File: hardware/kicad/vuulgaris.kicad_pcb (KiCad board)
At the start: 4 copper layers, 284.3 x 116.8 mm, 291 parts, among them J1 TFPUSH, J10 PJ-603_C41409498, J11 TYPE-C-31-M-12, J12 FACEPLATE 2x5 IDC, J2 PJ-376, J3 PJ-376, J4 PJ-376, J5 PJ-376, J6 PJ-376, J7 PJ-603_C41409498, J8 PJ-603_C41409498, J9 PJ-603_C41409498, Q1 J113 / MMBFJ113, Q2 J113 / MMBFJ113, SW1 SW_DPDT_FLAT, SW2 SW_DPDT_FLAT, SW4 12x12 tactile, SW5 12x12 tactile, SW6 12x12 tactile, SW7 12x12 tactile, SW8 12x12 tactile, SW9 12x12 tactile, U1 ES_DAISY_PATCH_SM_REV1, U101 V3205SD, U102 TL072_FLAT, U103 TL072_FLAT, U104 CD4046B, U106 TL072_FLAT, U201 V3205SD, U202 TL072_FLAT, U203 TL072_FLAT, U204 CD4046B, U206 TL072_FLAT, U3 MCP23017-E_SO, U301 TL084, U302 TL074, U4 MCP23017-E_SO, U401 TL084, U402 TL074, U5 AMS1117-3.3, U6 AMS1117-3.3, U7 DKM10E-12, U8 78L05, U9 OPA1688_FLAT

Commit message: hardware: 13 back-side parts had the FRONT land pattern -- fixed
Placing the preamp turned up a disagreement between my slot finder and
place.py, and chasing it found a board-killing bug that predates both.

KiCad applies no implicit mirror. Proven with kicad-cli pcb export svg: a pad
at footprint-local (0,+3) plots to the same absolute position whether its
footprint is on F.Cu or B.Cu. Front and back render identically, so the flip
has to be baked into the stored coordinates.

Thirteen parts on B.Cu still matched the library exactly, meaning they were
never mirrored -- only their layer names were rewritten. Q1, Q2, U101-U106 and
U201-U206: both V3205SD bucket brigades, both CD4046 clocks, five of six
TL072s, both transistors. The whole analogue block, every one of them soldered
mirror-image with pin 1 in the wrong corner.

Nothing caught it because place.py was applying an extra mirror of its own in
the position maths, so a half-flipped part measured correct -- two errors
cancelling inside the checks. The old comment claimed Gerber verification
against J7 and J11, but J7 is correctly mirrored and J11 is on the front, so
that check compared a double mirror against a single one. Meanwhile the pad
ANGLE check in the same file already assumed baked-in mirroring; the two halves
of place.py had contradicted each other for months.

Fixed: mir removed from place.py's position maths, the flip completed on all
106 half-flipped B.Cu footprints, and a new check that names any B.Cu footprint
whose asymmetric pads still match the library. Verified by half-flipping U102
on purpose and confirming the guard fires.

C507/C508 and RT502 re-placed against the corrected geometry. All 28 bypass
caps now within 5.0mm, pad overlaps none, body overlaps back to the
pre-existing four, 939/939 connections verified.
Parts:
- added C509: 100nF, vuulgaris:C0603, B.Cu at (280.6, 92.9)
- added C510: 100nF, vuulgaris:C0603, B.Cu at (272.3, 86.5)
- added C511: 1uF film, vuulgaris:C0603, B.Cu at (272.3, 89.9)
- added C512: 1uF film, vuulgaris:C0603, B.Cu at (280.7, 84.1)
- added R513: 1k3, vuulgaris:R0603, B.Cu at (310.5, 76.0)
- added R514: 1k, vuulgaris:R0603, B.Cu at (307.0, 76.0)
- added R515: 1k3, vuulgaris:R0603, B.Cu at (325.5, 76.0)
- added R516: 1k, vuulgaris:R0603, B.Cu at (322.0, 76.0)
- added R517: 1k, vuulgaris:R0603, B.Cu at (267.7, 78.5)
- added R518: 1k, vuulgaris:R0603, B.Cu at (286.7, 78.5)
- added R519: 100k, vuulgaris:R0603, B.Cu at (273.8, 83.4)
- added R520: 100k, vuulgaris:R0603, B.Cu at (283.7, 86.6)
- added R521: 2k2, vuulgaris:R0603, B.Cu at (275.3, 93.1)
- added R522: 2k2, vuulgaris:R0603, B.Cu at (283.7, 90.4)
- added RT503: 20k trim, vuulgaris:RES-ADJ-SMD_3224W, B.Cu at (268.8, 89.1)
- added RT504: 20k trim, vuulgaris:RES-ADJ-SMD_3224W, B.Cu at (287.2, 87.9)
- added U10: OPA1688_FLAT, vuulgaris:SOP-8_L4.9-W3.9-P1.27-LS6.0-BL, B.Cu at (278.0, 88.5)
- R511, R512: value 22R -> 4R7
- moved RT502 17.4 mm to (337.6, 73.7)
- moved C507 8.03 mm to (339.2, 69.5), turned to 0 degrees
- moved C508 5.46 mm to (348.2, 62.2)
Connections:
- C501 pad 1: /EXT_IN_L -> /EXT_AMP_OUT_L
- C502 pad 1: /EXT_IN_R -> /EXT_AMP_OUT_R
- J10 pad 4: /BBD_OUT_R -> /LINE_OUT_R
- J9 pad 4: /BBD_OUT_L -> /LINE_OUT_L
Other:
- board size 284.3 x 116.8 mm -> 284.3 x 326.3 mm

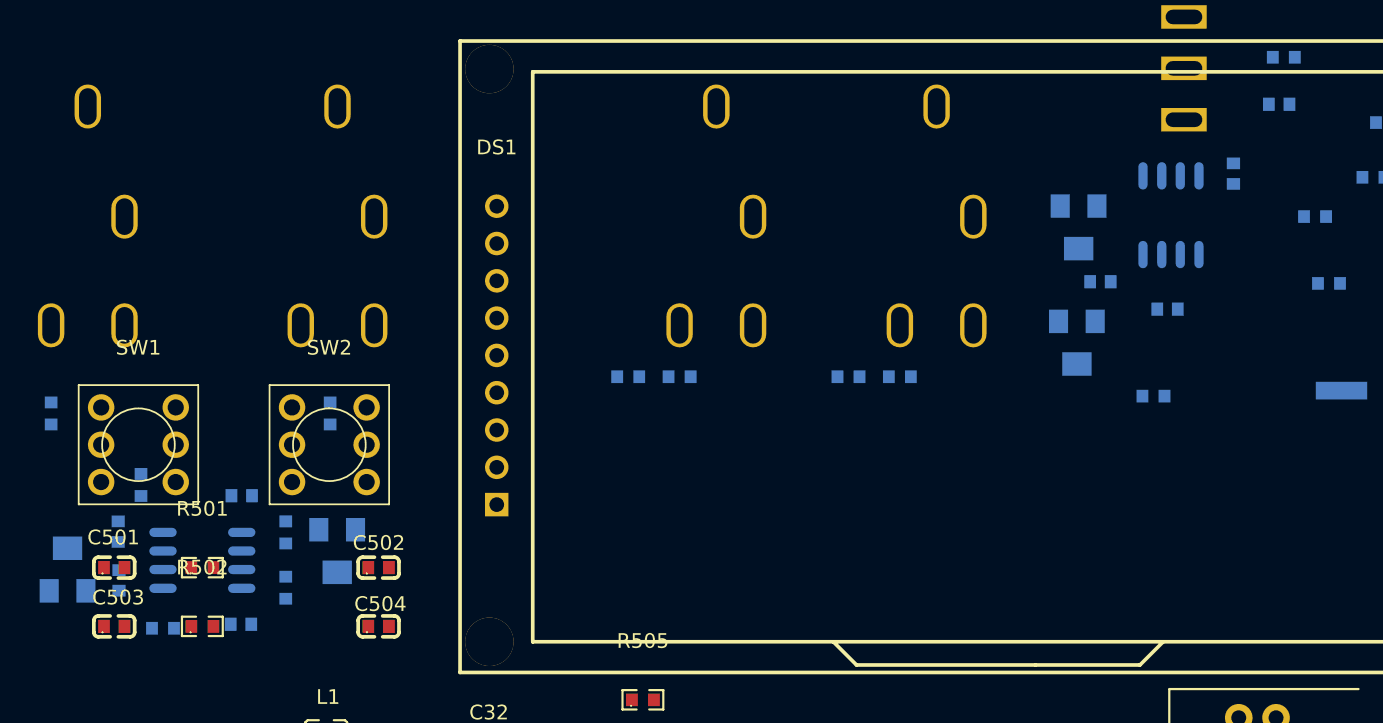
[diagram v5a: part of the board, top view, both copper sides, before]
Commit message: hardware: the 1uF "film" caps are 0805 X7R, because film was never possible
Fourteen caps carried the value "1uF film" in an 0603 footprint, which is not a
shippable part. SMD film tops out near 0.1uF in 1210; 1uF film is a leaded box
cap about 7x7mm on a 5mm pitch, hand-soldered, on a board whose hand-solder list
was cut to four genuinely unsourceable parts. What would actually have been
assembled is a Class II MLCC, so the value string was describing a wish.

They are now 1uF X7R 50V in C0805. Renaming alone would have been honest but
would have left the distortion: Class II voltage-coefficient nonlinearity scales
with the field across the dielectric, and a 1uF 50V part in 0805 has more and
thicker layers than a 1uF 16V part in 0603 being asked to swing a third of its
rating on a +/-4.75V Eurorack signal. 1uF C0G is the linear answer and is not an
option -- nothing below 2220, a few dollars each, fourteen of them would swallow
the board.

Eleven took the bigger footprint where they stood, checked against the corrected
back-side geometry. C505 turns 90 degrees to clear J6's body, C511 moves 3.4mm,
C512 0.25mm.

939/939 connections verified, all 28 bypass caps inside 5.0mm, no pad overlaps,
same-face body overlaps back to the pre-existing four.
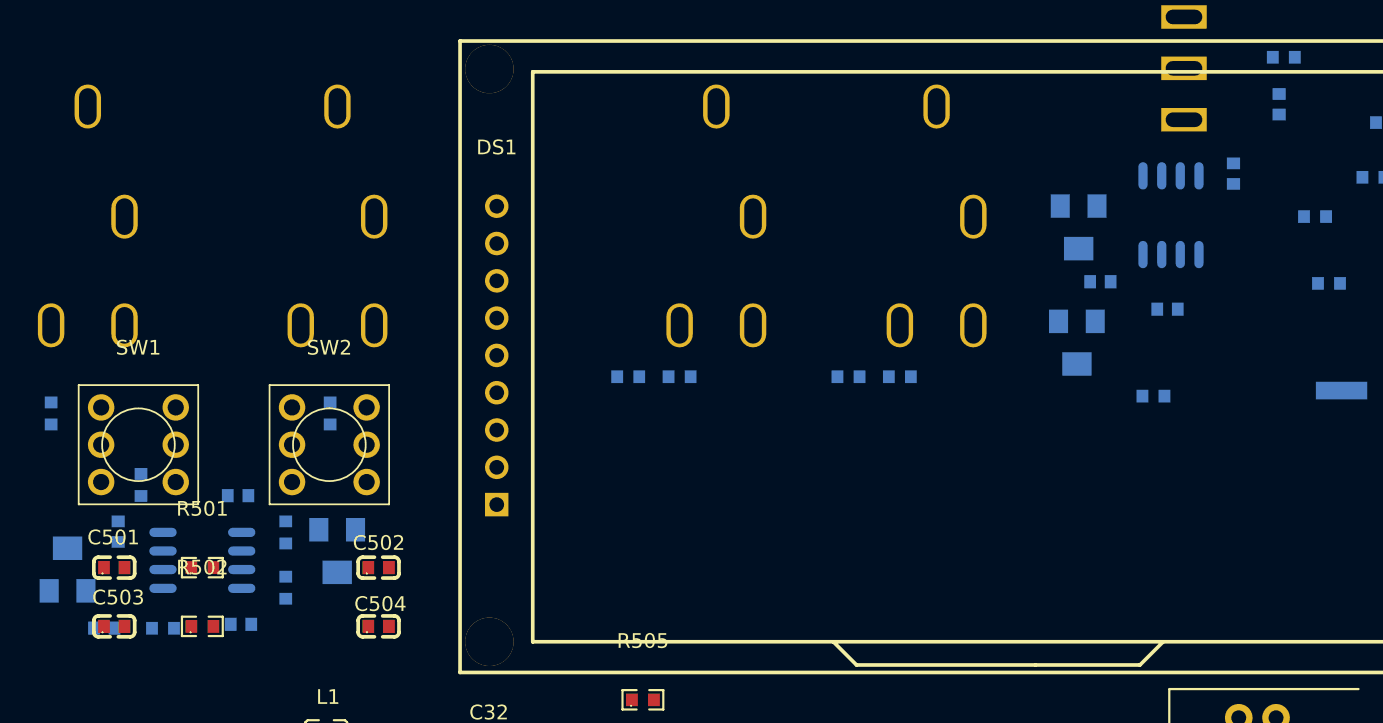
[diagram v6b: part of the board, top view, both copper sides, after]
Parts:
- moved C511 3.40 mm to (271.3, 93.1), turned to 0 degrees
- moved C512 0.25 mm to (280.4, 84.1)
- turned C505 to 90 degrees
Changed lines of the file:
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@@
   )
   (footprint "vuulgaris:C0603" (layer "B.Cu")
-    (at 280.68 84.1)
+    (at 280.43 84.1)
     (property "Sheetfile" "vuulgaris.kicad_sch")
     (property "Sheetname" "")
@@
   )
   (footprint "vuulgaris:C0603" (layer "B.Cu")
-    (at 272.32 89.87 90)
+    (at 271.32 93.12)
     (property "Sheetfile" "vuulgaris.kicad_sch")
     (property "Sheetname" "")
@@
     (fp_line (start 0.8 -0.4) (end -0.8 -0.4)
       (stroke (width 0.05) (type solid)) (layer "B.CrtYd"))
-    (pad "1" smd rect (at -0.7 0 90) (size 0.8 0.9) (layers "B.Cu" "B.Paste" "B.Mask")
+    (pad "1" smd rect (at -0.7 0) (size 0.8 0.9) (layers "B.Cu" "B.Paste" "B.Mask")
       (net 265 "/EXT_PROT_L") (pintype "passive"))
-    (pad "2" smd rect (at 0.7 0 90) (size 0.8 0.9) (layers "B.Cu" "B.Paste" "B.Mask")
+    (pad "2" smd rect (at 0.7 0) (size 0.8 0.9) (layers "B.Cu" "B.Paste" "B.Mask")
       (net 264 "/EXT_AMP_IN_L") (pintype "passive"))
     (model "lib/vuulgaris.3dshapes/C0603_L1.6-W0.8-H0.8.wrl"
@@
   )
   (footprint "vuulgaris:C0603" (layer "B.Cu")
-    (at 351.326 57.446)
+    (at 351.326 57.446 90)
     (property "Sheetfile" "vuulgaris.kicad_sch")
     (property "Sheetname" "")
@@
     (fp_line (start 0.8 0.4) (end 0.8 -0.4)
       (stroke (width 0.05) (type solid)) (layer "B.CrtYd"))
-    (pad "1" smd rect (at -0.7 0) (size 0.8 0.9) (layers "B.Cu" "B.Paste" "B.Mask")
+    (pad "1" smd rect (at -0.7 0 90) (size 0.8 0.9) (layers "B.Cu" "B.Paste" "B.Mask")
       (net 183 "/BBD_OUT_L") (pintype "passive"))
-    (pad "2" smd rect (at 0.7 0) (size 0.8 0.9) (layers "B.Cu" "B.Paste" "B.Mask")
+    (pad "2" smd rect (at 0.7 0 90) (size 0.8 0.9) (layers "B.Cu" "B.Paste" "B.Mask")
       (net 252 "/HP_IN_L") (pintype "passive"))
     (model "lib/vuulgaris.3dshapes/C0603_L1.6-W0.8-H0.8.wrl"

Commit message: hardware: restore the board outline -- pose.py had negated Edge.Cuts
The faceplate connector cutout lost its four straight edges. My unmirror pass
and pose.py split the board file into footprints by "start of one to start of
the next, with end-of-file as the last boundary", so the LAST footprint's block
ran to EOF and swallowed everything after it: Edge.Cuts, the zone, all of it.
The mirror transform then negated Y on all eight gr_line segments -- the outer
rectangle and the cutout both.

The four gr_arc corners survived because the negation regex wanted
(start ...) (end ...) adjacent and an arc carries a (mid ...) between them. So
the cutout kept its rounded corners and lost its edges, which is why nothing
automated caught it. Dylan spotted it by looking at the board.

place.py's fp_blocks walks to the balanced closing paren and always had this
right; pose.py rolled its own. pose.py now uses the balanced walk.

The same bug was also silently dropping pose.py's writes: it reported restoring
C505:rot90 and C511:rot0 and the board did not change. With the splitter fixed
those apply, and J1 -- which had been knocked to -90 in the working tree and is
rot 90 in every commit back to bda23e2 -- is back where it belongs.

Edge.Cuts restored from 7568060, the commit before the unmirror pass. Verified
surgical: only those 8 lines differ, 308 footprints on both sides.

outer rectangle x100-384.3 y50-166.81, cutout x310-334 y147.5-159.5, no
negative Y anywhere. place.py: clear of the cutout, pads inside the outline,
every B.Cu footprint mirrored, all 28 bypass caps inside 5.0mm, no pad
overlaps. pose.py --check: 0 drifted. 939/939 connections verified.
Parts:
- moved R519 7.55 mm to (266.3, 83.5)
- moved RT503 3.27 mm to (265.9, 90.6)
- moved C510 2.60 mm to (272.5, 89.1)
- moved R521 2.60 mm to (275.6, 95.7)
- moved C501 2.60 mm to (272.2, 91.6)
- moved C502 2.60 mm to (290.2, 91.6)
- moved C503 2.60 mm to (272.2, 95.6)
- moved C504 2.60 mm to (290.2, 95.6)
- moved C509 2.60 mm to (280.9, 95.4)
- moved R501 2.60 mm to (278.2, 91.6)
- moved R502 2.60 mm to (278.2, 95.6)
- moved R520 2.60 mm to (283.9, 89.2)
- moved U10 2.60 mm to (278.2, 91.1)
- moved R522 2.60 mm to (283.9, 93.0)
- moved RT504 2.60 mm to (287.4, 90.5)
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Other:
- board size 284.3 x 326.3 mm -> 284.3 x 116.8 mm

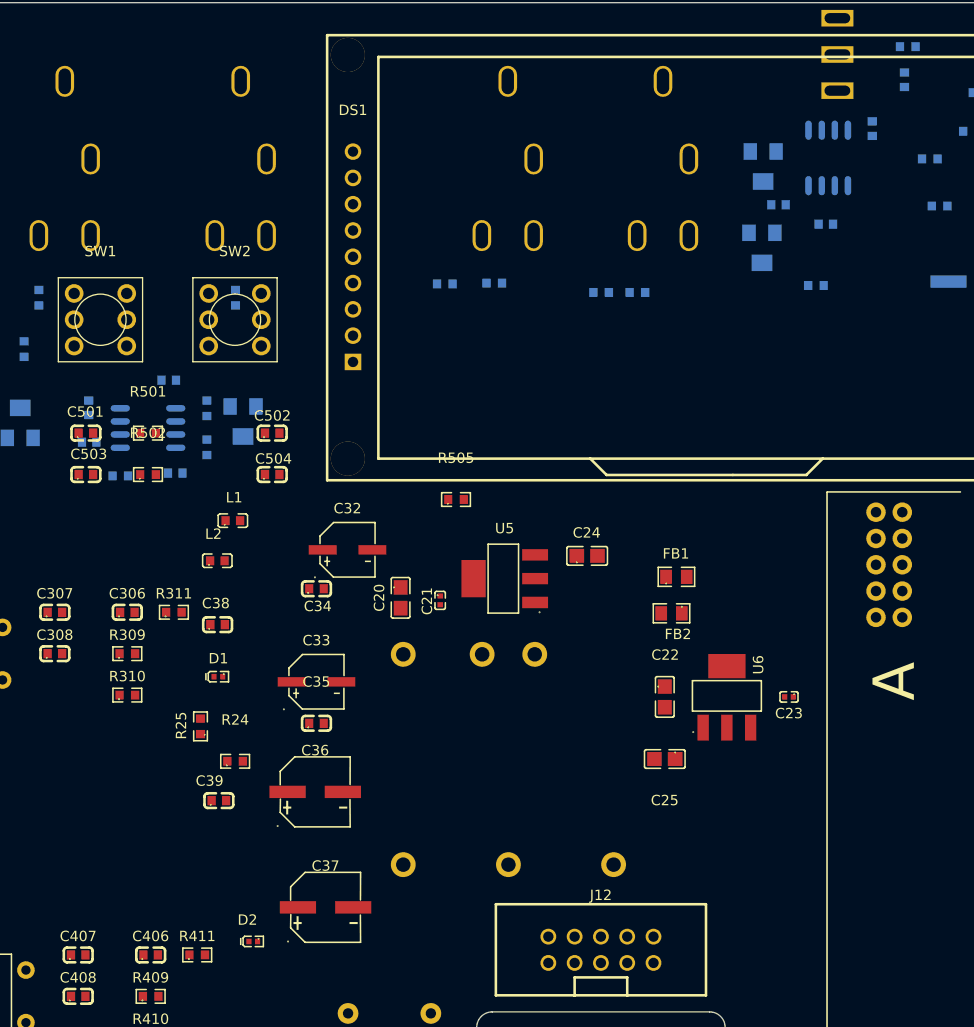
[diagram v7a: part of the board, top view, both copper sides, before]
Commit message: hardware: repair the board outline again, and guard it this time
The F8 wrote the damaged Edge.Cuts back. Commit f5b0823 had it correct on disk,
but Pcbnew was still holding the board it loaded before that fix, and saving
wrote its snapshot over the repair -- the snapshot I took immediately after the
F8, before running any tool, already has the negative Y. Fourth time the stale
in-memory board has cost work, and the first time it silently undid a fix.

What that looks like from the outside is an outline that needs moving: parts at
y 50-167, outline at y -50 to -167, drawn nowhere near the board.

Edge.Cuts sign-flipped back. place.py now validates the outline BEFORE measuring
anything against it -- negative coordinates, or most footprints falling outside
it, and it says so and says why it matters. "pads inside the outline" passes
trivially when the outline is somewhere else entirely, which is exactly how this
went unnoticed. Verified by re-breaking Edge.Cuts on purpose and confirming it
fires, then restoring.

Also C511 came out of the F8 0.36mm from U10 -- it was in free-placement.json,
so "board wins" kept the F8's position rather than the seed. Dropped and
re-seeded at 2.06mm.

board outline x 100..384.3 y 50..166.81, 1 interior cutout. All 14 coupling caps
swapped to C0805. 939/939 connections verified, all 28 bypass caps within 5.0mm,
no pad overlaps, back to the 11 pre-existing sub-1mm pairs.
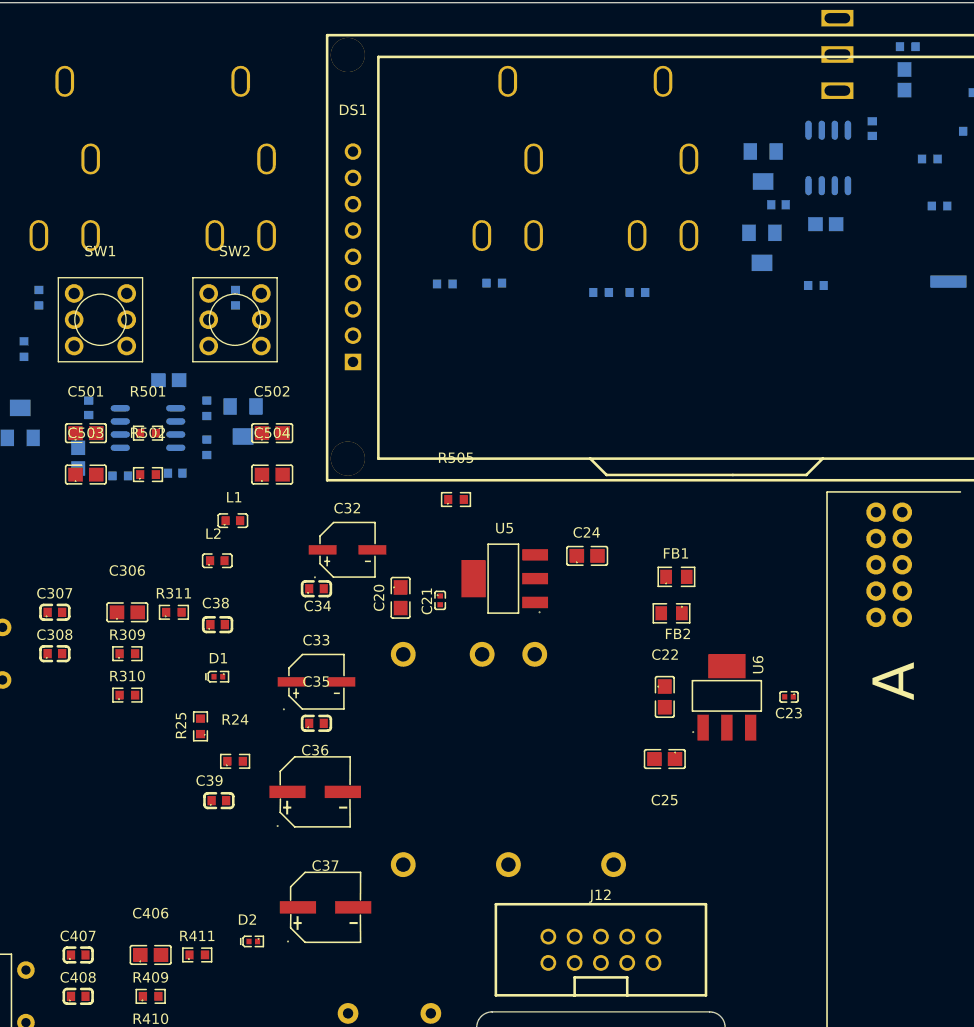
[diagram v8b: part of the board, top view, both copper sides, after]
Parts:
- C113, C120, C213, C220: value 1uF film -> 1uF X7R 50V
- C306, C406, C501, C502, C503, C504, C505, C506, C511, C512: value 1uF film -> 1uF X7R 50V; footprint vuulgaris:C0603 -> vuulgaris:C0805
- moved C511 1.87 mm to (271.5, 94.0), turned to 90 degrees
